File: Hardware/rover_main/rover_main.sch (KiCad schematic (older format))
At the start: 16 parts

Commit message: asig SDA and SCL
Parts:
- removed J?: VEML6075, symbol Connector:Conn_01x04_Female
- removed J?: DRIVERS, symbol Connector:Conn_01x10_Female
- added J4: DRIVERS, symbol Connector:Conn_01x06_Female
- added J8: PROG, symbol Connector_Generic:Conn_01x02
- gave numbers to parts that had none: 14
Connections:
- net labels removed: GPIO1, GPIO16, GPIO2, GPIO3
- wire segments 53 -> 49
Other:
- moved on the sheet: J2, J5, J6

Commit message: add footprints and manf#
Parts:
- removed C1, C3: 10uf, symbol Device:C_Small
- removed J5, J6: ESP32, symbol Connector:Conn_01x08_Female
- added C1, C2: 10uf, Capacitor_THT:CP_Radial_D5.0mm_P2.00mm, symbol Device:CP1_Small
- added U3: ESP32-CAM, Rf:ESP32-CAM, symbol electroniccats:ESP32-CAM
- C3: renamed from C2; footprint (none) -> Capacitor_THT:C_Disc_D5.0mm_W2.5mm_P5.00mm; manf# (none) -> K104K15X7RF53H5
- D1: footprint (none) -> Diode_THT:D_DO-15_P12.70mm_Horizontal; manf# (none) -> SB260-E3/54
- D2: footprint (none) -> LED_THT:LED_D5.0mm; manf# (none) -> VLCS5130
- J1: footprint (none) -> TerminalBlock:TerminalBlock_bornier-2_P5.08mm
- J2: footprint (none) -> Connector_PinHeader_2.54mm:PinHeader_1x04_P2.54mm_Vertical
- J3: footprint (none) -> Connector_PinHeader_2.54mm:PinHeader_1x08_P2.54mm_Vertical
- J4, J7: footprint (none) -> Connector_PinHeader_2.54mm:PinHeader_1x06_P2.54mm_Vertical
- J8: footprint (none) -> Connector_PinSocket_2.54mm:PinSocket_1x02_P2.54mm_Vertical
- R1: footprint (none) -> Resistor_THT:R_Axial_DIN0207_L6.3mm_D2.5mm_P10.16mm_Horizontal; manf# (none) -> CFR-25JT-52-330R
- U1: footprint Package_TO_SOT_SMD:SOT-223-3_TabPin2 -> Package_TO_SOT_THT:TO-220-3_Vertical
- U2: footprint (none) -> Batteries:charger_EC_3.3V_battery; manf# (none) -> EC
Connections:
- net +3V3: now also C2.1, U3.8 (3V3)
- net 3.3V-5V: now also U3.4 (VCC)
- net 5V: now also U3.9 (5V)
- net GND: now also C1.2, C2.2, U3.1 (GND), U3.10 (GND), U3.5 (GND)
- net GPIO0: now also U3.6 (IO0)
- net GPIO12: now also U3.11 (IO12)
- net GPIO13: now also U3.12 (IO13)
- net GPIO14: now also U3.14 (IO14)
- net GPIO15: now also U3.13 (IO15)
- net GPIO4: now also U3.16 (IO4)
- net RX: now also U3.3 (UnR)
- net SCL: now also U3.7 (IO16)
- net SDA: now also U3.15 (IO2)
- net TX: now also U3.2 (UoT)
- net at D1.1 (K), U1.3 (VI): now also C1.1
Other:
- moved on the sheet: J4, J7

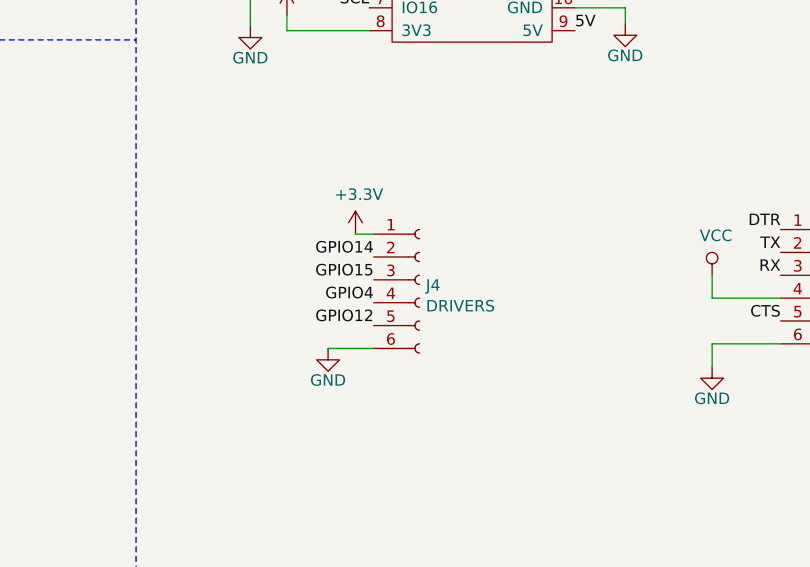
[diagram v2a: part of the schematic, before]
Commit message: antena wifi without cobre
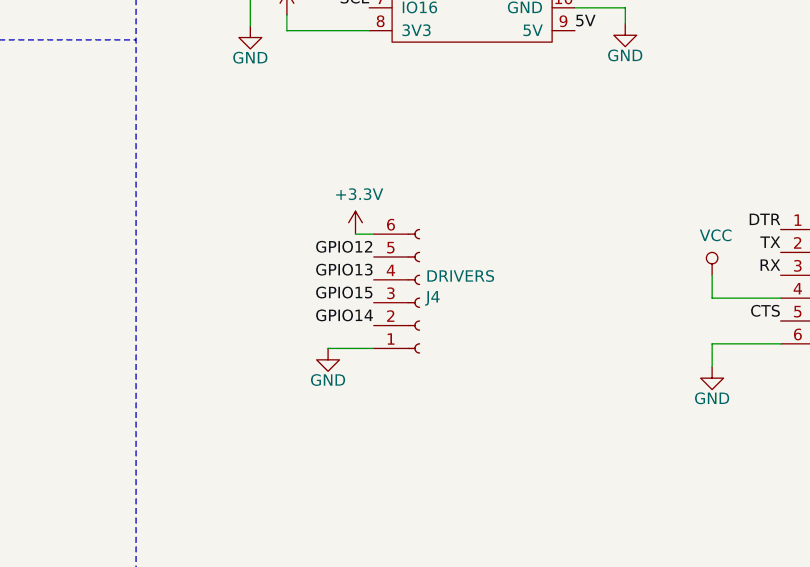
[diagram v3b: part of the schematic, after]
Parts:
- D1: footprint Diode_THT:D_DO-15_P12.70mm_Horizontal -> Diode_THT:D_A-405_P10.16mm_Horizontal
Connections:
- net +3V3: now also J4.6 (Pin_6); no longer J4.1 (Pin_1)
- net GND: now also J4.1 (Pin_1); no longer J4.6 (Pin_6)
- net GPIO13: now also J4.4 (Pin_4)
- net GPIO4: no longer J4.4 (Pin_4)
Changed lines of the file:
@@
 F 0 "D1" V 2846 1071 50  0000 R CNN
 F 1 "D_Schottky" V 2755 1071 50  0000 R CNN
-F 2 "Diode_THT:D_DO-15_P12.70mm_Horizontal" H 2800 1150 50  0001 C CNN
+F 2 "Diode_THT:D_A-405_P10.16mm_Horizontal" H 2800 1150 50  0001 C CNN
 F 3 "https://www.mouser.mx/datasheet/2/427/sb220-104141.pdf" H 2800 1150 50  0001 C CNN
 F 4 "SB260-E3/54" V 2800 1150 50  0001 C CNN "manf#"
@@
 	1    0    0    -1
 $EndComp
+Text Label 8040 3900 2    50   ~ 0
+GPIO14
 Text Label 8040 3800 2    50   ~ 0
-GPIO4
-Text Label 8040 3600 2    50   ~ 0
-GPIO14
-Text Label 8040 3700 2    50   ~ 0
 GPIO15
 Text Label 9820 3880 2    50   ~ 0
@@
 L Connector:Conn_01x06_Female J4
 U 1 1 5D28DF12
-P 8240 3700
-F 0 "J4" H 8268 3676 50  0000 L CNN
-F 1 "DRIVERS" H 8268 3585 50  0000 L CNN
-F 2 "Connector_PinHeader_2.54mm:PinHeader_1x06_P2.54mm_Vertical" H 8240 3700 50  0001 C CNN
-F 3 "~" H 8240 3700 50  0001 C CNN
-	1    8240 3700
-	1    0    0    -1
+P 8240 3800
+F 0 "J4" H 8268 3776 50  0000 L CNN
+F 1 "DRIVERS" H 8268 3685 50  0000 L CNN
+F 2 "Connector_PinHeader_2.54mm:PinHeader_1x06_P2.54mm_Vertical" H 8240 3800 50  0001 C CNN
+F 3 "~" H 8240 3800 50  0001 C CNN
+	1    8240 3800
+	1    0    0    1
 $EndComp
 Wire Wire Line
@@
 Text Label 8020 2510 2    50   ~ 0
 SCL
-Text Label 8040 3900 2    50   ~ 0
+Text Label 8040 3600 2    50   ~ 0
 GPIO12
 $Comp
@@
 Wire Wire Line
 	7500 2310 7500 2590
+Text Label 8040 3700 2    50   ~ 0
+GPIO13
 $EndSCHEMATC

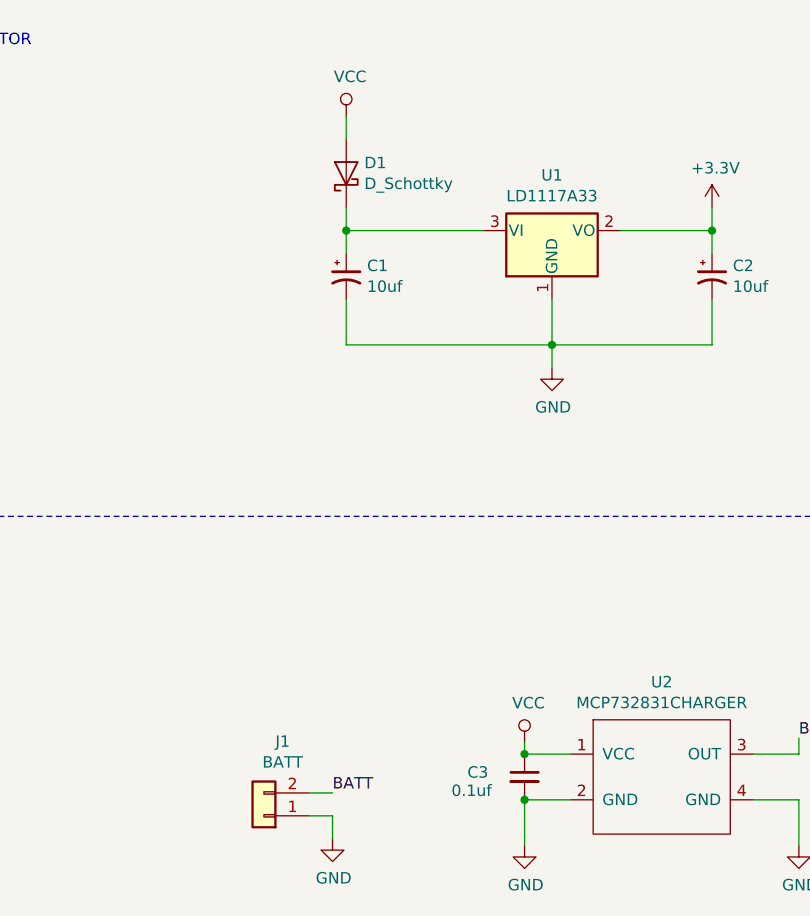
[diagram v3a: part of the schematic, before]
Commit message: change V batt
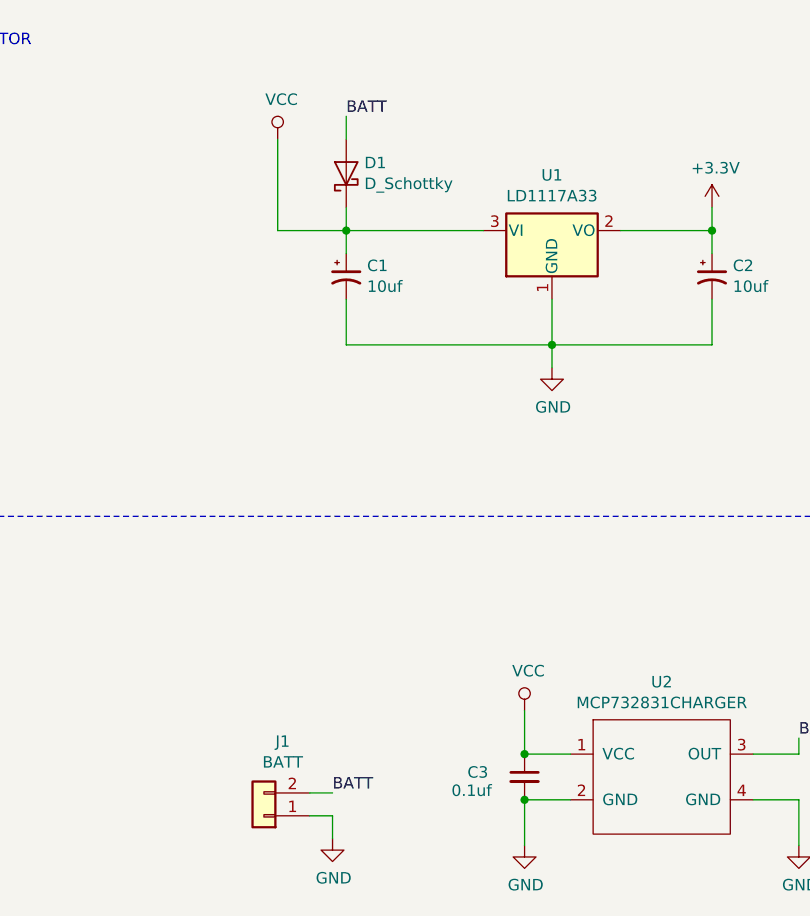
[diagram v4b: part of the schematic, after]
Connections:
- net BATT: now also D1.2 (A)
- net VCC: now also C1.1, D1.1 (K), U1.3 (VI); no longer D1.2 (A)
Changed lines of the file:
@@
 L power:VCC #PWR04
 U 1 1 5D24A1C2
-P 2800 900
-F 0 "#PWR04" H 2800 750 50  0001 C CNN
-F 1 "VCC" H 2817 1073 50  0000 C CNN
-F 2 "" H 2800 900 50  0001 C CNN
-F 3 "" H 2800 900 50  0001 C CNN
-	1    2800 900
+P 2500 1000
+F 0 "#PWR04" H 2500 850 50  0001 C CNN
+F 1 "VCC" H 2517 1173 50  0000 C CNN
+F 2 "" H 2500 1000 50  0001 C CNN
+F 3 "" H 2500 1000 50  0001 C CNN
+	1    2500 1000
 	1    0    0    -1
 $EndComp
@@
 L power:VCC #PWR05
 U 1 1 5D24F7E2
-P 3580 3640
-F 0 "#PWR05" H 3580 3490 50  0001 C CNN
-F 1 "VCC" H 3597 3813 50  0000 C CNN
-F 2 "" H 3580 3640 50  0001 C CNN
-F 3 "" H 3580 3640 50  0001 C CNN
-	1    3580 3640
-	1    0    0    -1
-$EndComp
-Wire Wire Line
-	3580 3640 3580 3690
+P 3580 3500
+F 0 "#PWR05" H 3580 3350 50  0001 C CNN
+F 1 "VCC" H 3597 3673 50  0000 C CNN
+F 2 "" H 3580 3500 50  0001 C CNN
+F 3 "" H 3580 3500 50  0001 C CNN
+	1    3580 3500
+	1    0    0    -1
+$EndComp
 Wire Wire Line
 	3580 3690 3780 3690
@@
 Text Label 8040 3700 2    50   ~ 0
 GPIO13
+Text Label 2800 900  0    50   ~ 0
+BATT
+Wire Wire Line
+	2500 1000 2500 1400
+Wire Wire Line
+	2500 1400 2800 1400
+Wire Wire Line
+	3580 3500 3580 3690
 $EndSCHEMATC

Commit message: add bast schematic
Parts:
- removed J8: PROG, Connector_PinSocket_2.54mm:PinSocket_1x02_P2.54mm_Vertical, symbol Connector_Generic:Conn_01x02
- added J10: Analog, Connector_PinHeader_2.54mm:PinHeader_1x12_P2.54mm_Vertical, symbol Connector_Generic:Conn_01x12
- added J5: GY-87, Connector_PinHeader_2.54mm:PinHeader_1x08_P2.54mm_Vertical, symbol Connector:Conn_01x08_Female
- added J6: PROG, Connector_PinHeader_2.54mm:PinHeader_1x03_P2.54mm_Vertical, symbol Connector:Conn_01x03_Female
- added J8: Digital, Connector_PinHeader_2.54mm:PinHeader_1x12_P2.54mm_Vertical, symbol Connector_Generic:Conn_01x12
- added J9: i2c, Connector_PinHeader_2.54mm:PinHeader_1x02_P2.54mm_Vertical, symbol Connector_Generic:Conn_01x02
- added JP1: Engine 2B, Jumper:SolderJumper-2_P1.3mm_Bridged_RoundedPad1.0x1.5mm, symbol Device:Jumper
- added JP10: Engine 2B, Connector_PinHeader_2.54mm:PinHeader_1x02_P2.54mm_Vertical, symbol Device:Jumper
- added JP11: SDE ESP, Jumper:SolderJumper-2_P1.3mm_Bridged_RoundedPad1.0x1.5mm, symbol Device:Jumper
- added JP12: SCL ESP, Jumper:SolderJumper-2_P1.3mm_Bridged_RoundedPad1.0x1.5mm, symbol Device:Jumper
- added JP2: Engine 1A, Jumper:SolderJumper-2_P1.3mm_Bridged_RoundedPad1.0x1.5mm, symbol Device:Jumper
- added JP3: Engine 2A, Jumper:SolderJumper-2_P1.3mm_Bridged_RoundedPad1.0x1.5mm, symbol Device:Jumper
- added JP4: Engine 1B, Jumper:SolderJumper-2_P1.3mm_Bridged_RoundedPad1.0x1.5mm, symbol Device:Jumper
- added JP5: SDA, Connector_PinHeader_2.54mm:PinHeader_1x02_P2.54mm_Vertical, symbol Device:Jumper
- added JP6: SCL, Connector_PinHeader_2.54mm:PinHeader_1x02_P2.54mm_Vertical, symbol Device:Jumper
- added JP7: Engine 1A, Connector_PinHeader_2.54mm:PinHeader_1x02_P2.54mm_Vertical, symbol Device:Jumper
- added JP8: Engine 1B, Connector_PinHeader_2.54mm:PinHeader_1x02_P2.54mm_Vertical, symbol Device:Jumper
- added JP9: Engine 2A, Connector_PinHeader_2.54mm:PinHeader_1x02_P2.54mm_Vertical, symbol Device:Jumper
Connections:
- net labels added: 10, 11, 12, 13, 2, 3, 4, 5, 6, 7, 8, 9, A0, A1, A2, A3, DRDY, FSYNC, GPIO12E, GPIO13E, GPIO14E, GPIO15E, INTA, RST, SCLB, SCLE, SDAB, SDAE, VCC-IN
- wire segments 51 -> 63
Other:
- moved on the sheet: J2, J3, J4, J7, U3

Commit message: Asig. places componets
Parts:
- removed J6: PROG, Connector_PinHeader_2.54mm:PinHeader_1x03_P2.54mm_Vertical, symbol Connector:Conn_01x03_Female
- added J6: PROG, Connector_PinSocket_2.54mm:PinSocket_1x02_P2.54mm_Vertical, symbol Connector:Conn_01x02_Female
- JP10, JP5, JP6, JP7, JP8, JP9: footprint Connector_PinHeader_2.54mm:PinHeader_1x02_P2.54mm_Vertical -> Jumper:SolderJumper-2_P1.3mm_Open_RoundedPad1.0x1.5mm
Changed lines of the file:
@@
 Text Label 7490 1550 2    50   ~ 0
 GPIO0
-$Comp
-L Connector:Conn_01x03_Female J6
-U 1 1 5D496659
-P 7690 1550
-F 0 "J6" H 7718 1576 50  0000 L CNN
-F 1 "PROG" H 7718 1485 50  0000 L CNN
-F 2 "Connector_PinHeader_2.54mm:PinHeader_1x03_P2.54mm_Vertical" H 7690 1550 50  0001 C CNN
-F 3 "~" H 7690 1550 50  0001 C CNN
-	1    7690 1550
-	1    0    0    -1
-$EndComp
 Wire Wire Line
 	7390 1750 7390 1650
@@
 F 0 "JP5" H 10100 4664 50  0000 C CNN
 F 1 "SDA" H 10100 4573 50  0000 C CNN
-F 2 "Connector_PinHeader_2.54mm:PinHeader_1x02_P2.54mm_Vertical" H 10100 4400 50  0001 C CNN
+F 2 "Jumper:SolderJumper-2_P1.3mm_Open_RoundedPad1.0x1.5mm" H 10100 4400 50  0001 C CNN
 F 3 "~" H 10100 4400 50  0001 C CNN
 	1    10100 4400
@@
 F 0 "JP6" H 10100 5064 50  0000 C CNN
 F 1 "SCL" H 10100 4973 50  0000 C CNN
-F 2 "Connector_PinHeader_2.54mm:PinHeader_1x02_P2.54mm_Vertical" H 10100 4800 50  0001 C CNN
+F 2 "Jumper:SolderJumper-2_P1.3mm_Open_RoundedPad1.0x1.5mm" H 10100 4800 50  0001 C CNN
 F 3 "~" H 10100 4800 50  0001 C CNN
 	1    10100 4800
@@
 F 0 "JP10" H 10100 6654 50  0000 C CNN
 F 1 "Engine 2B" H 10100 6563 50  0000 C CNN
-F 2 "Connector_PinHeader_2.54mm:PinHeader_1x02_P2.54mm_Vertical" H 10100 6390 50  0001 C CNN
+F 2 "Jumper:SolderJumper-2_P1.3mm_Open_RoundedPad1.0x1.5mm" H 10100 6390 50  0001 C CNN
 F 3 "~" H 10100 6390 50  0001 C CNN
 	1    10100 6390
@@
 F 0 "JP9" H 10100 6264 50  0000 C CNN
 F 1 "Engine 2A" H 10100 6173 50  0000 C CNN
-F 2 "Connector_PinHeader_2.54mm:PinHeader_1x02_P2.54mm_Vertical" H 10100 6000 50  0001 C CNN
+F 2 "Jumper:SolderJumper-2_P1.3mm_Open_RoundedPad1.0x1.5mm" H 10100 6000 50  0001 C CNN
 F 3 "~" H 10100 6000 50  0001 C CNN
 	1    10100 6000
@@
 F 0 "JP8" H 10100 5864 50  0000 C CNN
 F 1 "Engine 1B" H 10100 5773 50  0000 C CNN
-F 2 "Connector_PinHeader_2.54mm:PinHeader_1x02_P2.54mm_Vertical" H 10100 5600 50  0001 C CNN
+F 2 "Jumper:SolderJumper-2_P1.3mm_Open_RoundedPad1.0x1.5mm" H 10100 5600 50  0001 C CNN
 F 3 "~" H 10100 5600 50  0001 C CNN
 	1    10100 5600
 	1    0    0    -1
 $EndComp
-Text Label 9800 5200 2    50   ~ 0
+Text Label 9800 6000 2    50   ~ 0
 A3
-Text Label 10400 5200 0    50   ~ 0
+Text Label 10400 5600 0    50   ~ 0
 GPIO12
 $Comp
@@
 F 0 "JP7" H 10100 5464 50  0000 C CNN
 F 1 "Engine 1A" H 10100 5373 50  0000 C CNN
-F 2 "Connector_PinHeader_2.54mm:PinHeader_1x02_P2.54mm_Vertical" H 10100 5200 50  0001 C CNN
+F 2 "Jumper:SolderJumper-2_P1.3mm_Open_RoundedPad1.0x1.5mm" H 10100 5200 50  0001 C CNN
 F 3 "~" H 10100 5200 50  0001 C CNN
 	1    10100 5200
 	1    0    0    -1
 $EndComp
-Text Label 10400 5600 0    50   ~ 0
+Text Label 10400 5200 0    50   ~ 0
 GPIO13
 Text Label 10400 6000 0    50   ~ 0
@@
 Wire Wire Line
 	8980 4790 9330 4790
-Text Label 7490 1450 2    50   ~ 0
-GPIO0
 $Comp
 L Device:Jumper JP2
@@
 Text Label 5290 6000 2    50   ~ 0
 VCC-IN
+Text Label 9800 5600 2    50   ~ 0
+11
+Text Label 9800 5200 2    50   ~ 0
+A1
 Text Label 9800 6390 2    50   ~ 0
-11
-Text Label 9800 5600 2    50   ~ 0
-A2
-Text Label 9800 6000 2    50   ~ 0
-A1
+9
+$Comp
+L Connector:Conn_01x02_Female J6
+U 1 1 5D5E84D2
+P 7690 1550
+F 0 "J6" H 7718 1526 50  0000 L CNN
+F 1 "PROG" H 7718 1435 50  0000 L CNN
+F 2 "Connector_PinSocket_2.54mm:PinSocket_1x02_P2.54mm_Vertical" H 7690 1550 50  0001 C CNN
+F 3 "~" H 7690 1550 50  0001 C CNN
+	1    7690 1550
+	1    0    0    -1
+$EndComp
 $EndSCHEMATC

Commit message: RE-ROUTEO
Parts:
- removed J2: BME280, Connector_PinHeader_2.54mm:PinHeader_1x04_P2.54mm_Vertical, symbol Connector:Conn_01x04_Female
- added J2: BME280, Connector_PinHeader_2.54mm:PinHeader_1x06_P2.54mm_Vertical, symbol Connector:Conn_01x06_Female
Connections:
- net +3V3: now also J2.1 (Pin_1)
- net GND: now also J2.2 (Pin_2)
- net SCL: now also J2.3 (Pin_3)
- net SDA: now also J2.4 (Pin_4)
- no-connect marks 2 -> 4
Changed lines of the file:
@@
 	-1   0    0    1
-$EndComp
-$Comp
-L Connector:Conn_01x04_Female J2
-U 1 1 5D2155B1
-P 2210 6310
-F 0 "J2" H 2238 6286 50  0000 L CNN
-F 1 "BME280" H 2238 6195 50  0000 L CNN
-F 2 "Connector_PinHeader_2.54mm:PinHeader_1x04_P2.54mm_Vertical" H 2210 6310 50  0001 C CNN
-F 3 "~" H 2210 6310 50  0001 C CNN
-	1    2210 6310
-	1    0    0    -1
 $EndComp
 Text Label 2010 6410 2    50   ~ 0
@@
 L power:GND #PWR024
 U 1 1 5D4B3B5B
-P 7720 5730
-F 0 "#PWR024" H 7720 5480 50  0001 C CNN
-F 1 "GND" H 7720 5590 50  0000 C CNN
-F 2 "" H 7720 5730 50  0001 C CNN
-F 3 "" H 7720 5730 50  0001 C CNN
-	1    7720 5730
+P 7400 5600
+F 0 "#PWR024" H 7400 5350 50  0001 C CNN
+F 1 "GND" H 7400 5460 50  0000 C CNN
+F 2 "" H 7400 5600 50  0001 C CNN
+F 3 "" H 7400 5600 50  0001 C CNN
+	1    7400 5600
 	1    0    0    -1
 $EndComp
@@
 Text Label 7900 5380 2    50   ~ 0
 7
-Text Label 7900 5480 2    50   ~ 0
-8
 Text Label 7900 5580 2    50   ~ 0
 9
-Wire Wire Line
-	7900 4780 7720 4780
-Wire Wire Line
-	7720 4780 7720 5730
 Text Label 8980 5590 0    50   ~ 0
 10
@@
 Text Label 8980 5290 0    50   ~ 0
 13
-Text Label 8980 5190 0    50   ~ 0
-A0
 Text Label 8980 5090 0    50   ~ 0
 A1
@@
 	1    0    0    -1
 $EndComp
+$Comp
+L Connector:Conn_01x06_Female J2
+U 1 1 5D49D204
+P 2210 6410
+F 0 "J2" H 2238 6386 50  0000 L CNN
+F 1 "BME280" H 2238 6295 50  0000 L CNN
+F 2 "Connector_PinHeader_2.54mm:PinHeader_1x06_P2.54mm_Vertical" H 2210 6410 50  0001 C CNN
+F 3 "~" H 2210 6410 50  0001 C CNN
+	1    2210 6410
+	1    0    0    -1
+$EndComp
+Wire Wire Line
+	7400 4780 7400 5600
+Wire Wire Line
+	7400 4780 7900 4780
+Text Label 7900 5480 2    50   ~ 0
+8
+Text Label 8980 5190 0    50   ~ 0
+A0
+NoConn ~ 2010 6610
+NoConn ~ 2010 6710
 $EndSCHEMATC

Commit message: Update traces
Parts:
- U2: symbol electroniccats:MCP732831CHARGER -> rover_main-rescue:MCP732831CHARGER-electroniccats
- U3: symbol electroniccats:ESP32-CAM -> rover_main-rescue:ESP32-CAM-electroniccats
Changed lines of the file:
@@
 	3280 6160 3570 6160
 $Comp
-L electroniccats:MCP732831CHARGER U2
+L rover_main-rescue:MCP732831CHARGER-electroniccats U2
 U 1 1 5D24ED12
 P 4180 3790
@@
 $EndComp
 $Comp
-L electroniccats:ESP32-CAM U3
+L rover_main-rescue:ESP32-CAM-electroniccats U3
 U 1 1 5D363E9F
 P 9080 1350
